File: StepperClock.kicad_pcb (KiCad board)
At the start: 4 copper layers, 108.7 x 64.4 mm, 24 parts, among them J1 Hour1, J2 Hour0, J3 Minute1, J4 Minute0, J5 Second1, J6 Second0, J7 +12V, SW1 TZ, U1 TFT Display, U2 5V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

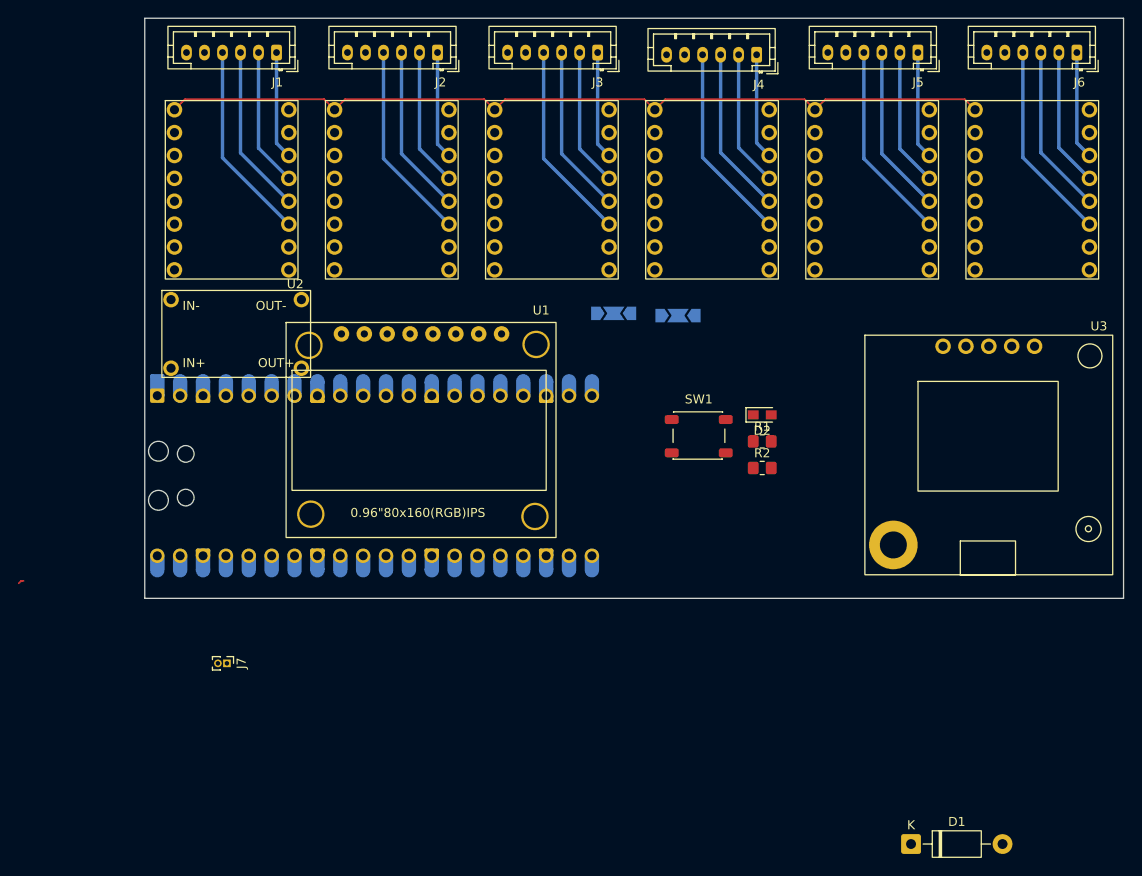
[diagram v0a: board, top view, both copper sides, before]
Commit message: Remove backup directory from repository Finish board routing
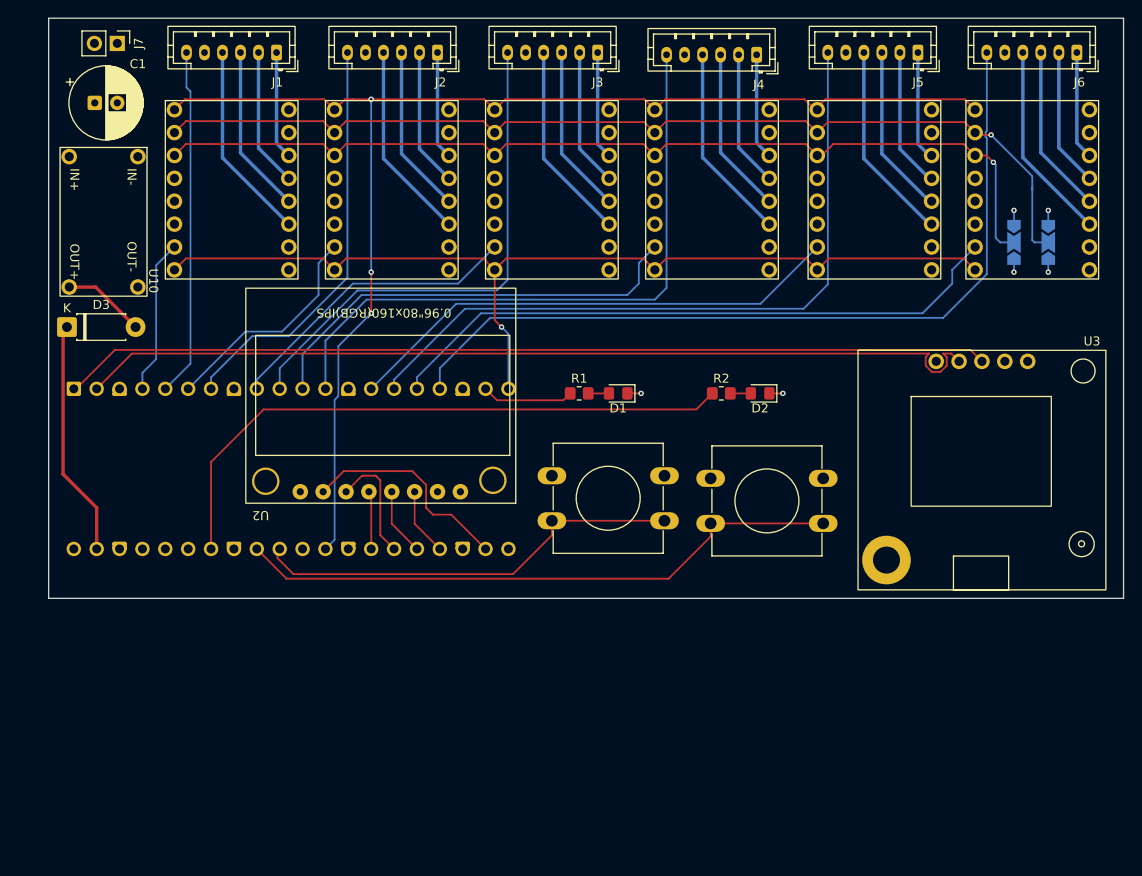
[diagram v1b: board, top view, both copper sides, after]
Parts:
- removed A1: RaspberryPi_Pico, Module:RaspberryPi_Pico_Common_Unspecified
- added C1: 47uF, Capacitor_THT:CP_Radial_D8.0mm_P2.50mm, F.Cu at (84.9, 52.1)
- added D3: 1N5819, Diode_THT:D_DO-41_SOD81_P7.62mm_Horizontal, F.Cu at (81.8, 77.0)
- added SW2: Debug, Button_Switch_THT:SW_PUSH-12mm, F.Cu at (153.3, 93.8)
- added U2: TFT Display, .tls-footprints:TFT_Display_.94in, F.Cu at (125.5, 95.2)
- D1: value 1N4001 -> LED; footprint Diode_THT:D_DO-41_SOD81_P10.16mm_Horizontal -> Diode_SMD:D_0805_2012Metric_Pad1.15x1.40mm_HandSolder
- D2: footprint LED_SMD:LED_miniPLCC_2315_Handsoldering -> Diode_SMD:D_0805_2012Metric_Pad1.15x1.40mm_HandSolder
- J7: footprint Connector_PinHeader_1.00mm:PinHeader_1x02_P1.00mm_Vertical -> Connector_PinHeader_2.54mm:PinHeader_1x02_P2.54mm_Vertical
- R1, R2: value R -> 1k
- SW1: footprint .tls-footprints:SW_PB_Wurth_5x4mm -> Button_Switch_THT:SW_PUSH-12mm
- U1: value TFT Display -> RaspberryPi_Pico; footprint .tls-footprints:TFT_Display_.94in -> .tls-footprints:RaspberryPi_Pico_Common_THT; moved to B.Cu
- U6: value Min1 -> Minute1
- U7: value Min0 -> Minute0
- U8: value Sec1 -> Second1
- U9: value Sec0 -> Second0
- moved J7 69.9 mm to (87.4, 45.5)
- moved D1 59.7 mm to (143.0, 84.3), turned to 180 degrees
- moved JP1 48.9 mm to (190.8, 67.6), turned to 90 degrees
- moved JP2 38.2 mm to (186.9, 67.6), turned to 90 degrees
- moved U1 30.3 mm to (82.5, 83.8), turned to -90 degrees
- moved R1 21.0 mm to (138.7, 84.3)
- moved SW1 16.9 mm to (135.6, 93.5)
- moved U10 16.3 mm to (89.7, 58.0), turned to -90 degrees
- moved R2 9.45 mm to (154.4, 84.3)
- moved D2 2.40 mm to (158.8, 84.3), turned to 180 degrees
- moved U3 1.84 mm to (183.4, 80.8)
- moved U8 0.25 mm to (165.1, 52.8)
- renumbered U2 to U10
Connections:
- D1 pad 1: Net-(A1-VSYS) -> GND
- D1 pad 2: +5V -> Net-(D1-A)
- J5 pad 6: unconnected-(J5-Pin_6-Pad6) -> /Sec1Home
- JP1 pad 1: +5V -> GND
- JP1 pad 3: GND -> +3V3
- JP2 pad 1: +5V -> GND
- JP2 pad 3: GND -> +3V3
- R1 pad 1: /Debug -> /DebugLED
- R1 pad 2: Net-(D2-A) -> Net-(D1-A)
- R2 pad 1: +3V3 -> /MotorDebug
- R2 pad 2: /TZOffset -> Net-(D2-A)
- SW1 pad 2: /TZOffset -> /TZ_PB
- U1 pad 1: GND -> /GPSRx
- U1 pad 2: +3V3 -> /GPSTx
- U1 pad 3: /SCK -> GND
- U1 pad 4: /MOSI -> /Hour1Step
- U1 pad 5: /TFT_Reset -> /Hour1Home
- U1 pad 6: /TFT_D/~{C} -> /Hour0Step
- U1 pad 7: /TFT_Select -> /Hour0Home
- U1 pad 8: unconnected-(U1-BLK-Pad8) -> GND
- U10 pad 3: +5V -> Net-(D3-A)
- U3 pad 2: /PicoRx -> /GPSTx
- U3 pad 3: /PicoTx -> /GPSRx
- U4 pad 1: /Enable -> /MotorEnable
- U4 pad 10: +5V -> +3V3
- U5 pad 1: /Enable -> /MotorEnable
- U5 pad 10: +5V -> +3V3
- U6 pad 1: /Enable -> /MotorEnable
- U6 pad 10: +5V -> +3V3
- U7 pad 1: /Enable -> /MotorEnable
- U7 pad 10: +5V -> +3V3
- U8 pad 1: /Enable -> /MotorEnable
- U8 pad 10: +5V -> +3V3
- U9 pad 1: /Enable -> /MotorEnable
- U9 pad 10: +5V -> +3V3
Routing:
- net /MotorEnable: track 0.00 -> 145.8 mm, vias 0 -> 3
- net /MS1: track 0.00 -> 111.8 mm, vias 0 -> 1
- net /Direction: track 0.00 -> 108.0 mm, vias 0 -> 1
- net /MS2: track 0.00 -> 107.5 mm, vias 0 -> 1
- net /GPSRx: track 0.00 -> 103.2 mm
- net /GPSTx: track 0.00 -> 102.1 mm
- net /Enable: track 93.7 -> 0.00 mm
- net /Sec0Home: track 0.00 -> 92.1 mm
- net /Sec1Home: track 0.00 -> 79.3 mm
- net /Min0Home: track 0.00 -> 71.5 mm
- net /Sec0Step: track 0.00 -> 70.1 mm
- net /MotorDebug: track 0.00 -> 68.5 mm
- net /DebugPB: track 0.00 -> 67.7 mm
- net /Min1Home: track 0.00 -> 56.9 mm
- net /Sec1Step: track 0.00 -> 56.1 mm
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- added copper zone on In2.Cu, net +3V3
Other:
- board size 108.7 x 64.4 mm -> 119.4 x 64.4 mm
